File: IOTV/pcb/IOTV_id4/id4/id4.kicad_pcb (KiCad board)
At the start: 2 copper layers, 109.2 x 73.7 mm, 57 parts, among them Q1 S8050, Q10 S8050, Q11 S8050, Q12 S8050, Q13 S8050, Q14 S8050, Q15 S8050, Q2 S8050, Q3 S8050, Q4 S8050, Q5 S8050, Q6 S8050, Q7 S8050, Q8 S8050, Q9 S8050, SW1 SW_Push, SW2 SW_Push, SW3 SW_Push, U1 ESP32_DevKit_V1_DOIT, U2 DFR0299

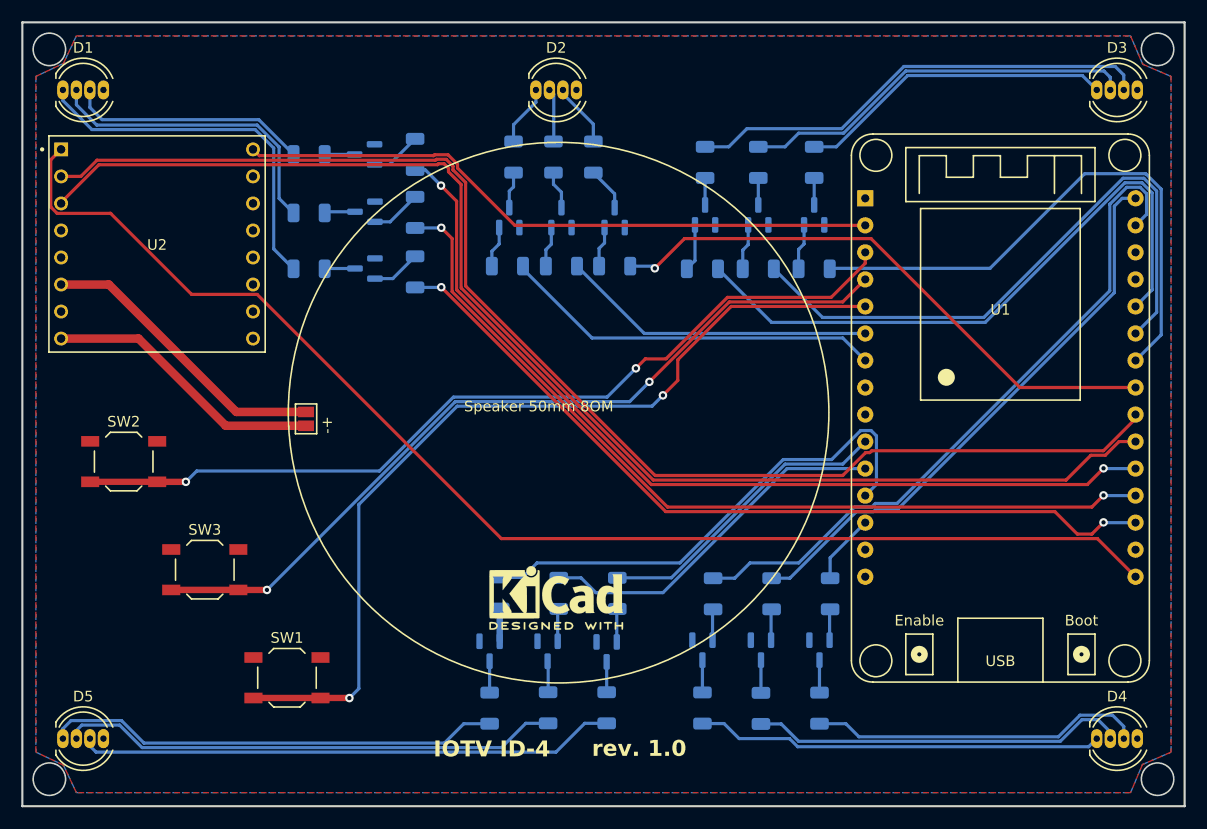
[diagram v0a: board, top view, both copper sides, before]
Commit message: pcb id4 - rezonit OK
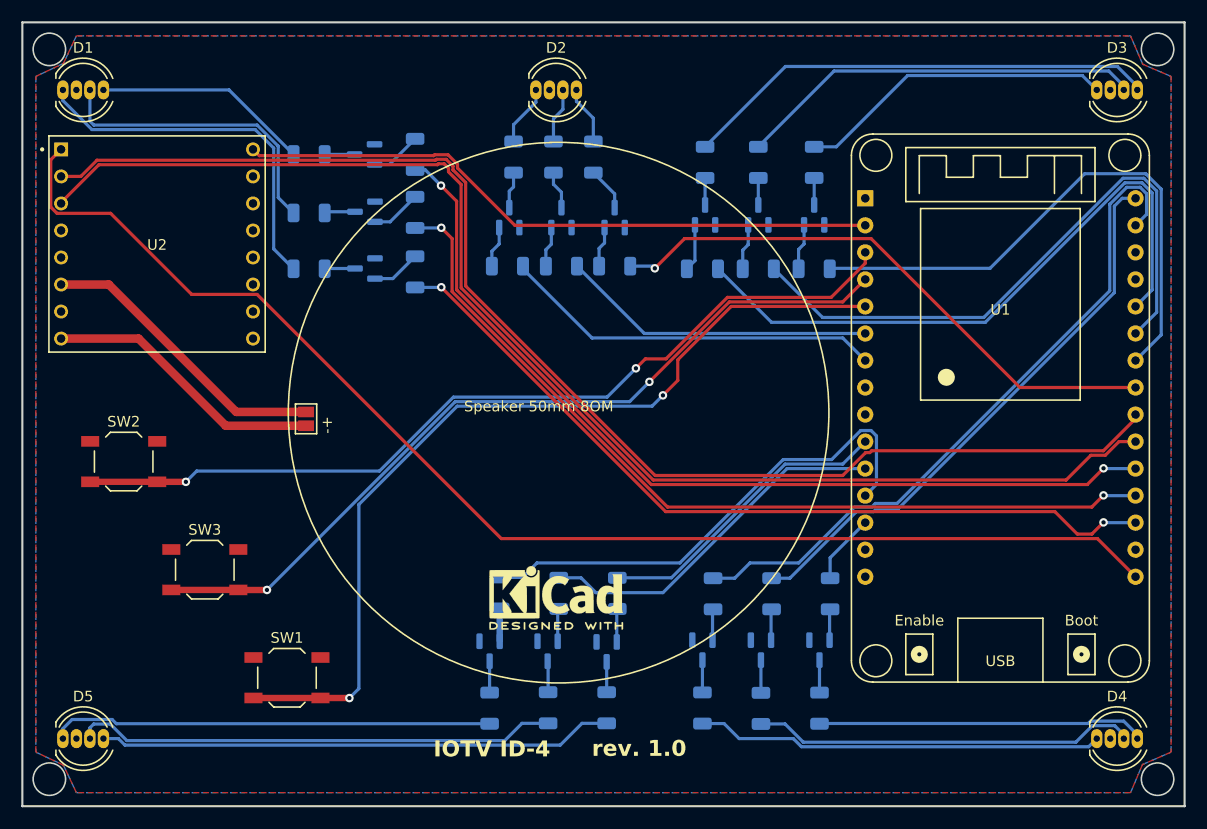
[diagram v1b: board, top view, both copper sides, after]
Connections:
- D1 pad 2: Net-(D1-GK) -> VCC_5
- D1 pad 3: Net-(D1-BK) -> Net-(D1-GK)
- D1 pad 4: VCC_5 -> Net-(D1-BK)
- D2 pad 2: Net-(D2-GK) -> VCC_5
- D2 pad 3: Net-(D2-BK) -> Net-(D2-GK)
- D2 pad 4: VCC_5 -> Net-(D2-BK)
- D3 pad 2: Net-(D3-GK) -> VCC_5
- D3 pad 3: Net-(D3-BK) -> Net-(D3-GK)
- D3 pad 4: VCC_5 -> Net-(D3-BK)
- D4 pad 2: Net-(D4-GK) -> VCC_5
- D4 pad 3: Net-(D4-BK) -> Net-(D4-GK)
- D4 pad 4: VCC_5 -> Net-(D4-BK)
- D5 pad 2: Net-(D5-GK) -> VCC_5
- D5 pad 3: Net-(D5-BK) -> Net-(D5-GK)
- D5 pad 4: VCC_5 -> Net-(D5-BK)
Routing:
- net Net-(D1-BK): track 22.6 -> 20.4 mm
- net Net-(D5-BK): track 50.6 -> 48.4 mm
- net Net-(D5-GK): track 47.1 -> 45.5 mm
- net Net-(D5-RK): track 43.0 -> 41.6 mm
- net Net-(D3-GK): track 37.5 -> 38.2 mm
- net Net-(D4-GK): track 35.5 -> 36.2 mm
- net Net-(D4-BK): track 31.5 -> 30.8 mm
- net Net-(D3-BK): track 44.2 -> 44.8 mm
- net Net-(D2-BK): track 6.03 -> 5.51 mm

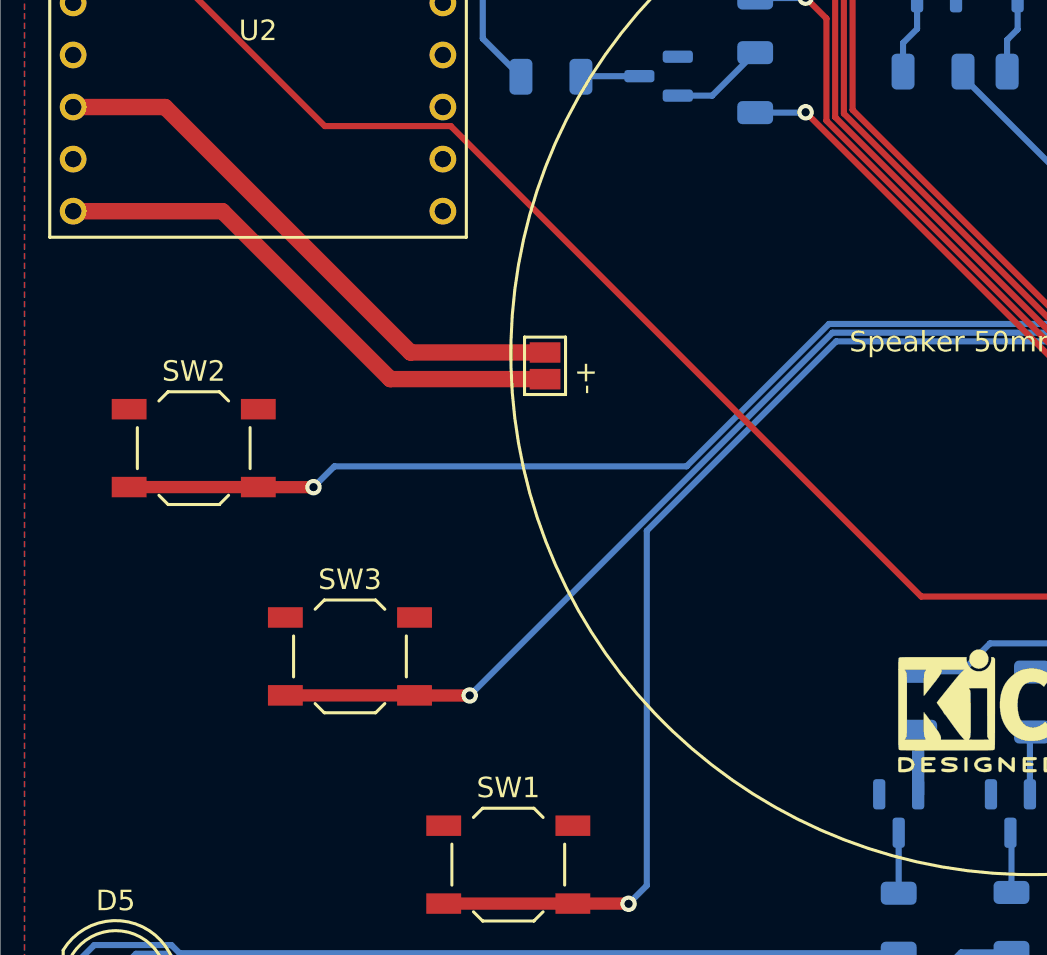
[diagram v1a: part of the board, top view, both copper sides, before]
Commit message: pcd id 4
на кнопках исправлен контакт с 5в на 3,3в
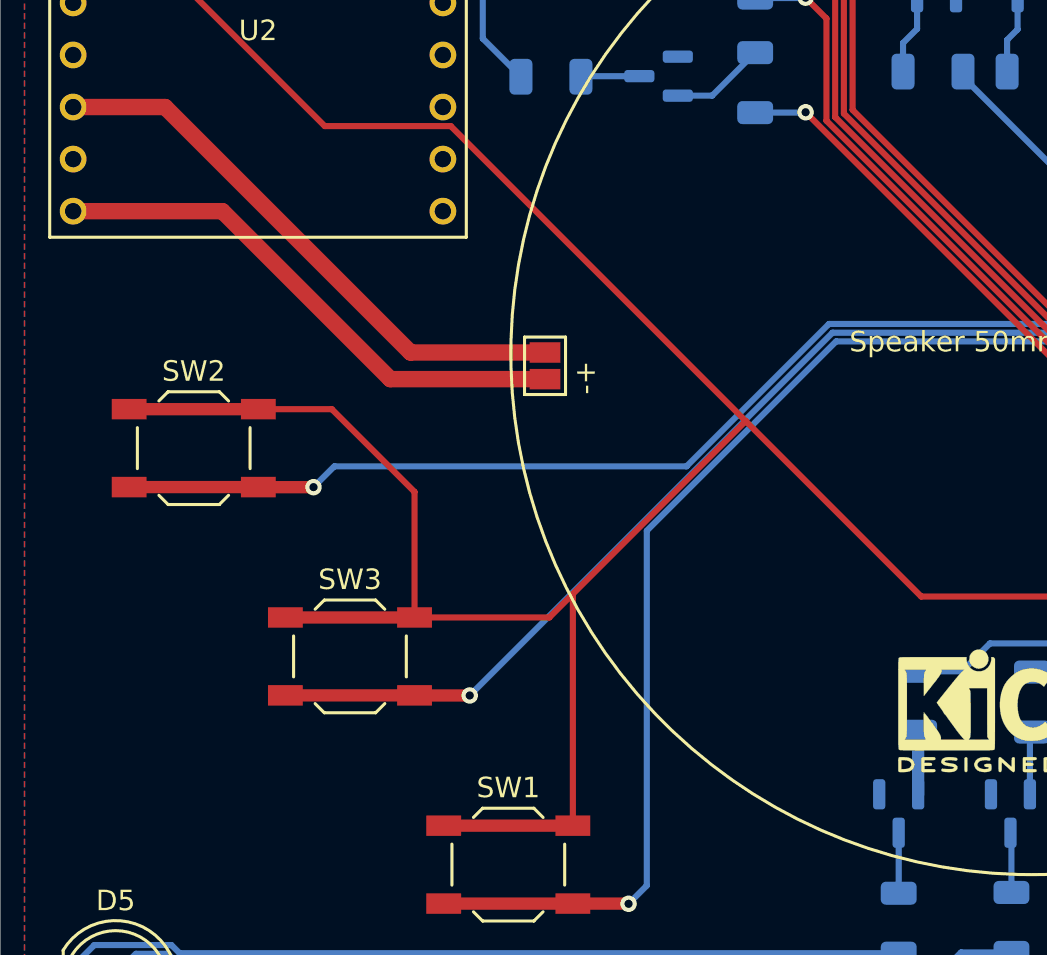
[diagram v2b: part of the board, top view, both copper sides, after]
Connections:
- SW1 pad 1: VCC_5 -> VCC_3.3
- SW2 pad 1: VCC_5 -> VCC_3.3
- SW3 pad 1: VCC_5 -> VCC_3.3
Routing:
- net VCC_3.3: track 122.2 -> 187.9 mm
